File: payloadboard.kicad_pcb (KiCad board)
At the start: 2 copper layers, 46.8 x 46.8 mm, 15 parts, among them J1 TFM-110-12-L-D-A, J2 FLE-105-01-G-DV-A, J3 Micro_SD_Card, Q4 MMBT2907

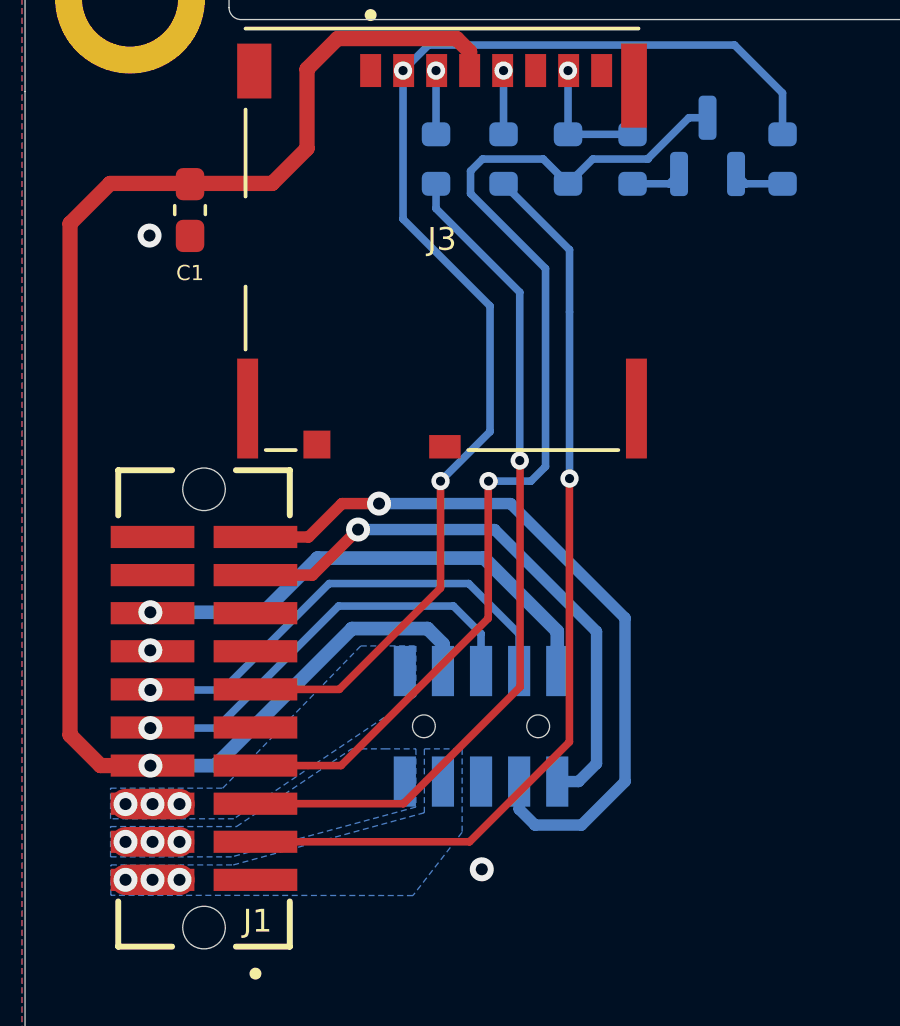
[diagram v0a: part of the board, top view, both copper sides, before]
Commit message: Rerouted traces for better GND connection
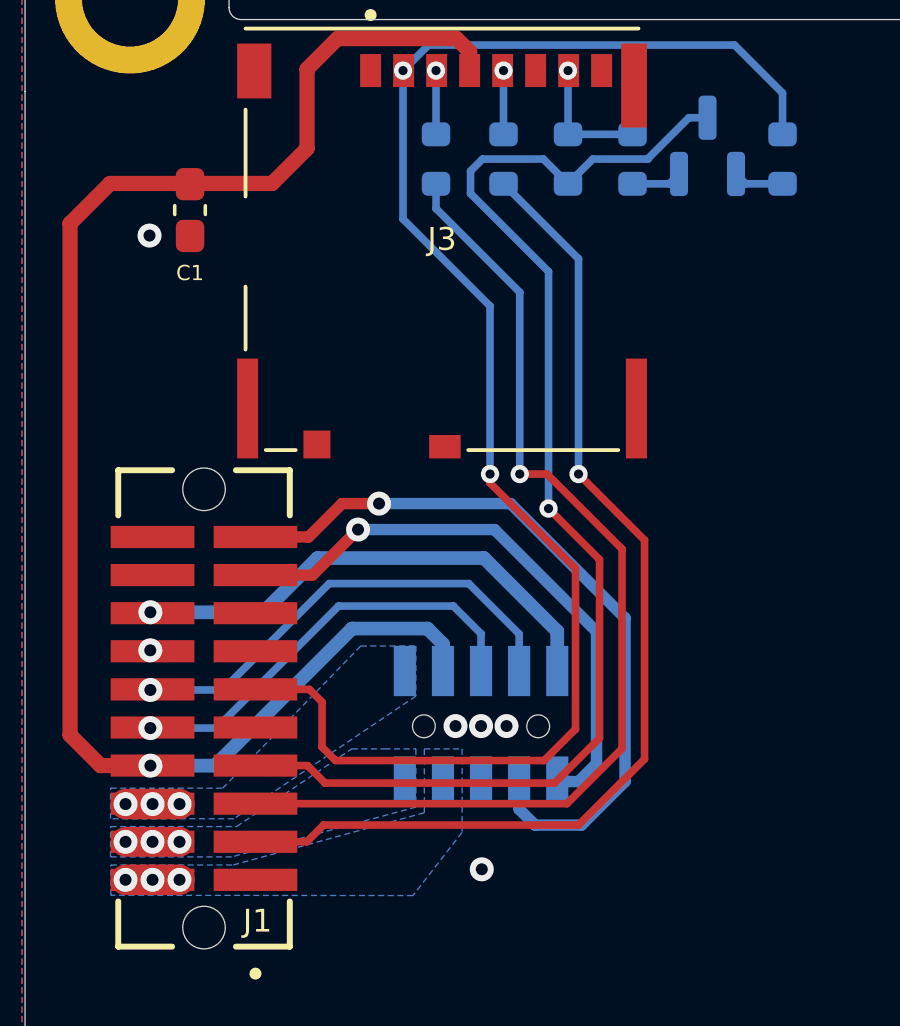
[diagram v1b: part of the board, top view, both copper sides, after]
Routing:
- net SD_CS: track 41.7 -> 52.3 mm
- net MOSI: track 28.4 -> 34.9 mm
- net MISO: track 36.7 -> 42.4 mm
- net SCK: track 31.4 -> 35.2 mm
- net GND: vias 3 -> 6
